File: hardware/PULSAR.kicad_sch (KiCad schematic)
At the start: 5 parts, among them U1 AP2112K-3.3, U2 SS49E, U3 CD74HC4067M

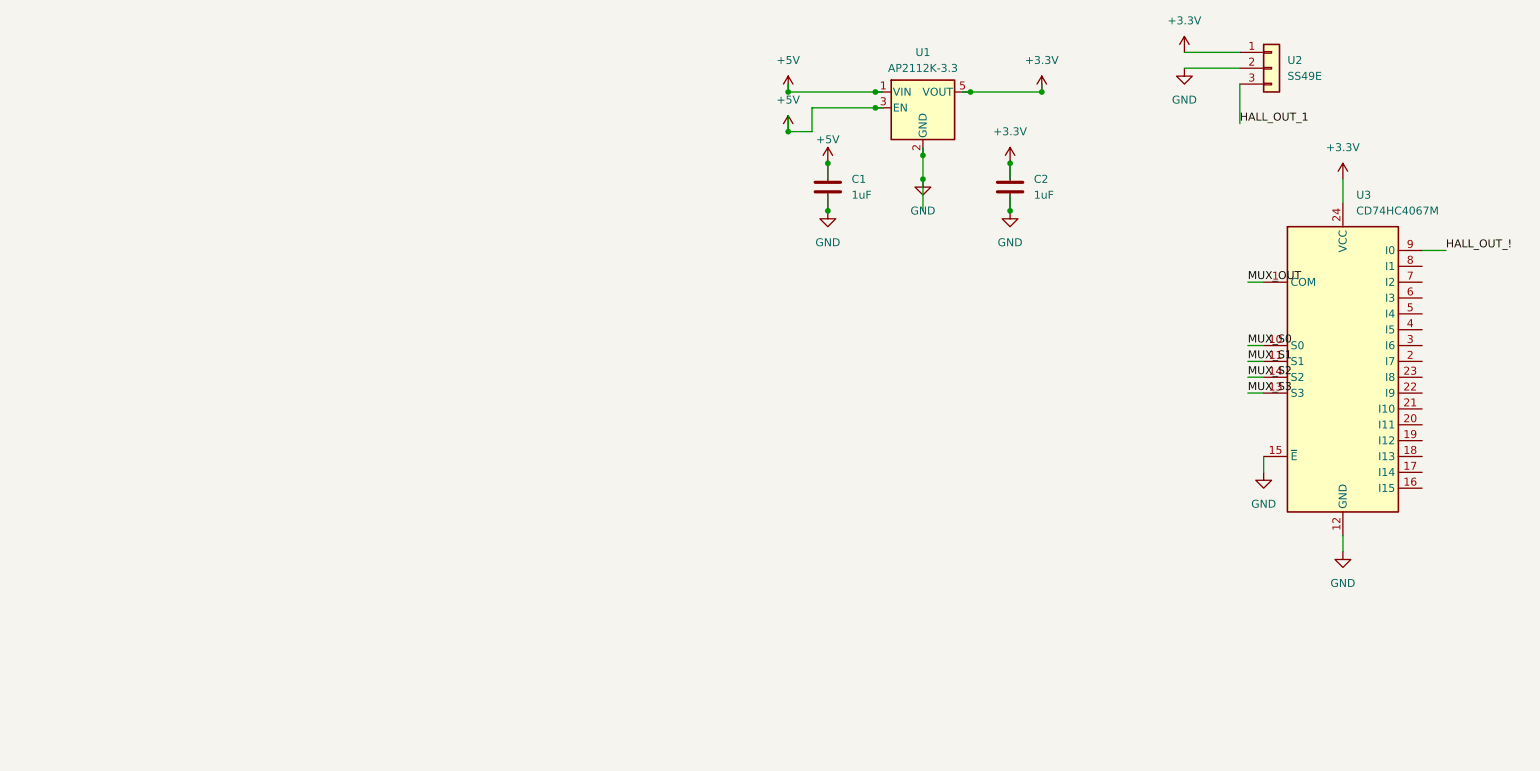
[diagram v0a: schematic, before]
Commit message: feat: add ADS8688 ADC schematic with SPI signals and analog input from MUX
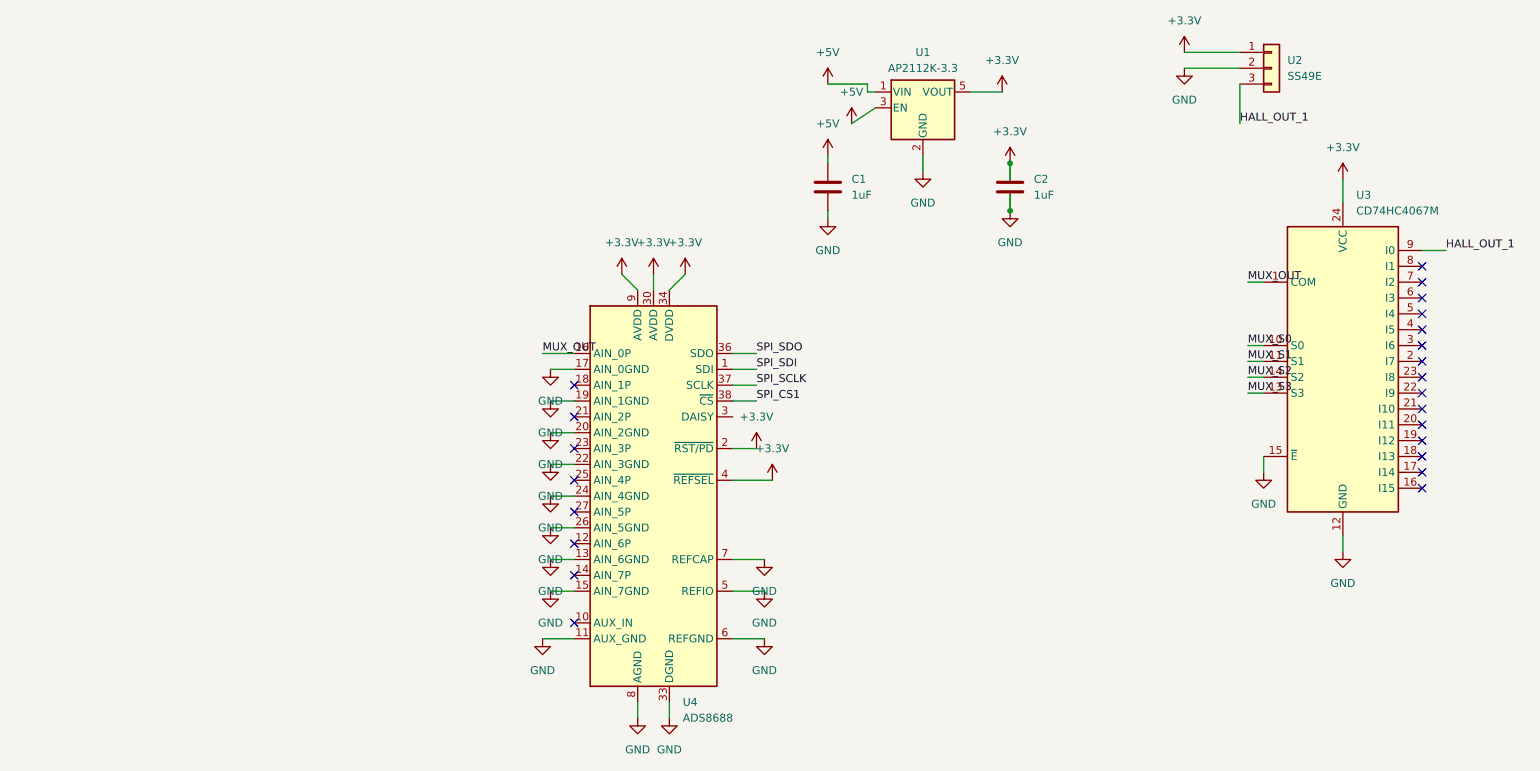
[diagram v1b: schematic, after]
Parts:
- added U4: ADS8688, Package_SO:TSSOP-38_4.4x9.7mm_P0.5mm, symbol Analog_ADC:ADS8688
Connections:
- net HALL_OUT_! is gone; now on net HALL_OUT_1: U3.9 (I0)
- net +3.3V: now also U4.2 (~{RST/PD}), U4.30 (AVDD), U4.34 (DVDD), U4.4 (~{REFSEL}), U4.9 (AVDD)
- net GND: now also U4.11 (AUX_GND), U4.13 (AIN_6GND), U4.15 (AIN_7GND), U4.17 (AIN_0GND), U4.19 (AIN_1GND), U4.20 (AIN_2GND), U4.22 (AIN_3GND), U4.24 (AIN_4GND), U4.26 (AIN_5GND), U4.28 (AGND), U4.29 (AGND), U4.31 (AGND), U4.32 (AGND), U4.33 (DGND), U4.5 (REFIO), U4.6 (REFGND), U4.7 (REFCAP), U4.8 (AGND)
- net MUX_OUT: now also U4.16 (AIN_0P)
- new net SPI_CS1: U4.38 (~{CS})
- new net SPI_SCLK: U4.37 (SCLK)
- new net SPI_SDI: U4.1 (SDI)
- new net SPI_SDO: U4.36 (SDO)
- no-connect marks 0 -> 23

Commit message: feat: add OrangeCrab connector with SPI, MUX and power signals
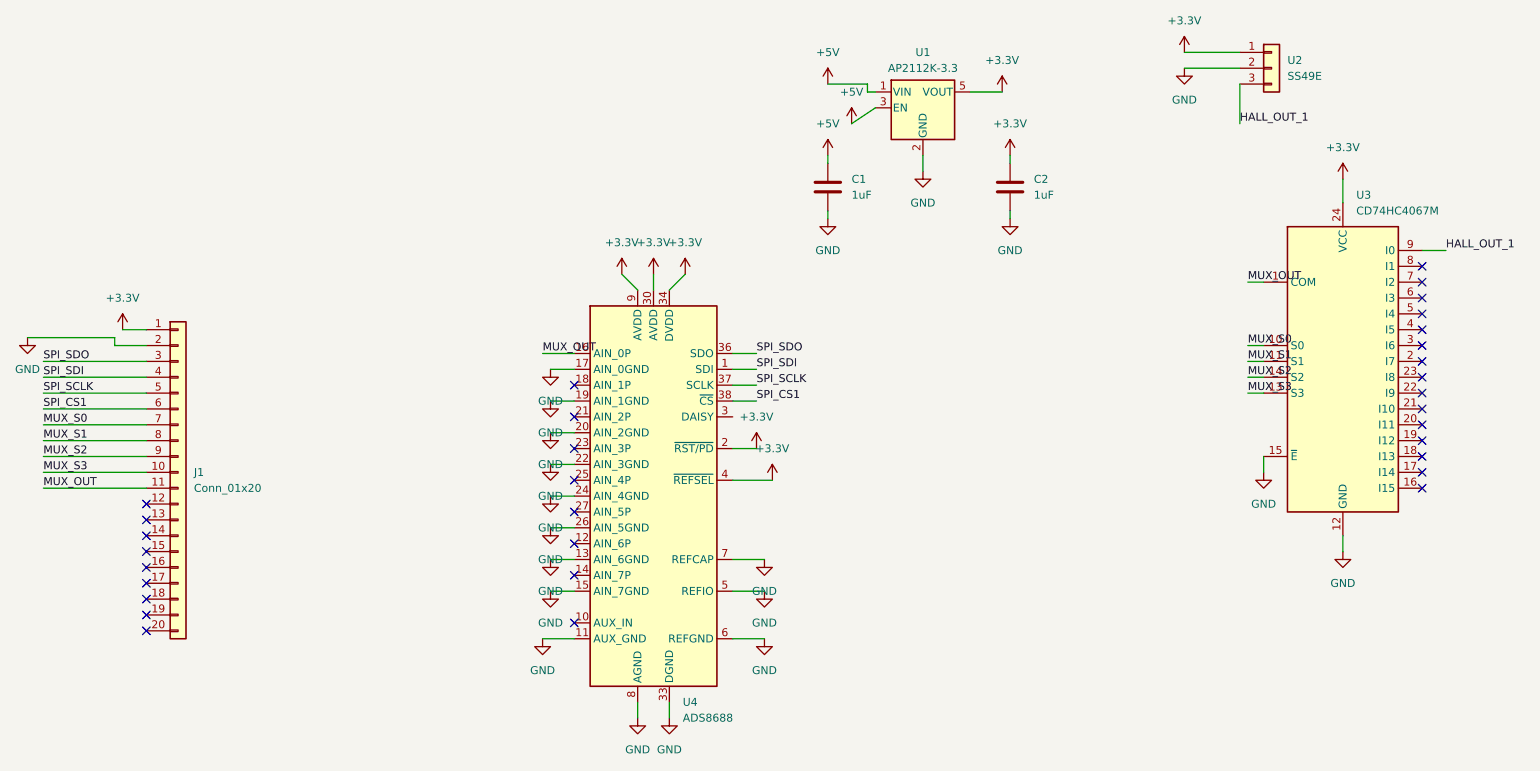
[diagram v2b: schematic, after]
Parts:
- added J1: Conn_01x20, symbol Connector_Generic:Conn_01x20
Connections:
- net +3.3V: now also J1.1 (Pin_1)
- net GND: now also J1.2 (Pin_2)
- net MUX_OUT: now also J1.11 (Pin_11)
- net MUX_S0: now also J1.7 (Pin_7)
- net MUX_S1: now also J1.8 (Pin_8)
- net MUX_S2: now also J1.9 (Pin_9)
- net MUX_S3: now also J1.10 (Pin_10)
- net SPI_CS1: now also J1.6 (Pin_6)
- net SPI_SCLK: now also J1.5 (Pin_5)
- net SPI_SDI: now also J1.4 (Pin_4)
- net SPI_SDO: now also J1.3 (Pin_3)
- no-connect marks 23 -> 32
